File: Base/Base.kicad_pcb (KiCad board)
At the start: 2 copper layers, 0 parts

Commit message: add components
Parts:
- added C1: 22u, Capacitor_THT:CP_Radial_D5.0mm_P2.50mm, F.Cu at (103.0, 97.0)
- added D1: LED, LED_THT:LED_D5.0mm_Clear, F.Cu at (135.0, 102.5)
- added D2: LED, LED_THT:LED_D5.0mm_Clear, F.Cu at (125.0, 102.5)
- added J1: USB_C_Receptacle_PowerOnly_6P, Connector_USB:USB_C_Receptacle_GCT_USB4135-GF-A_6P_TopMnt_Horizontal, F.Cu at (83.5, 78.0)
- added J2: Conn_01x04_Socket, Connector_PinSocket_2.54mm:PinSocket_1x04_P2.54mm_Vertical, F.Cu at (97.0, 89.4)
- added R1: 5k1, Resistor_THT:R_Axial_DIN0207_L6.3mm_D2.5mm_P10.16mm_Horizontal, F.Cu at (89.3, 80.0)
- added R2: 5k1, Resistor_THT:R_Axial_DIN0207_L6.3mm_D2.5mm_P10.16mm_Horizontal, F.Cu at (89.4, 76.0)
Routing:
- net (no net): vias 10 -> 14
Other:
- board outline added: 100 x 40 mm

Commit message: update pcb
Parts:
- added G***: LOGO, LOGO, F.Cu at (176.0, 90.0)

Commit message: RC1
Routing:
- net Net-(D1-K): track 0.00 -> 98.6 mm
- net Net-(D1-A): track 0.00 -> 42.4 mm
- net Net-(J2-Pin_4): track 0.00 -> 32.8 mm
- net Net-(D2-A): track 0.00 -> 31.3 mm
- net Net-(J1-CC1): track 0.00 -> 3.51 mm
- net Net-(J1-CC2): track 0.00 -> 3.43 mm
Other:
- board text added: "JLCJLCJLCJLC"

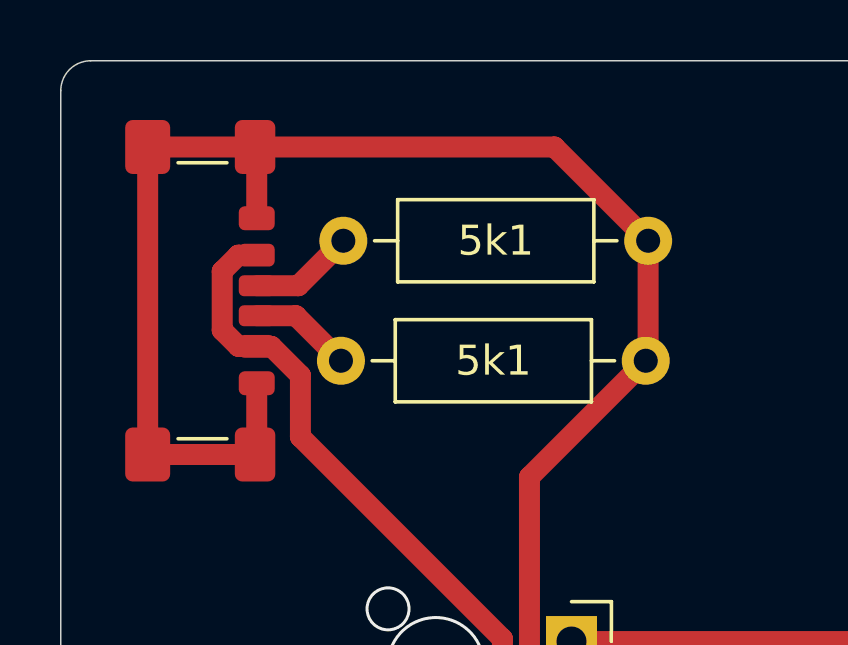
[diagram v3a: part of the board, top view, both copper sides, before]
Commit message: RC2, un-ground shield
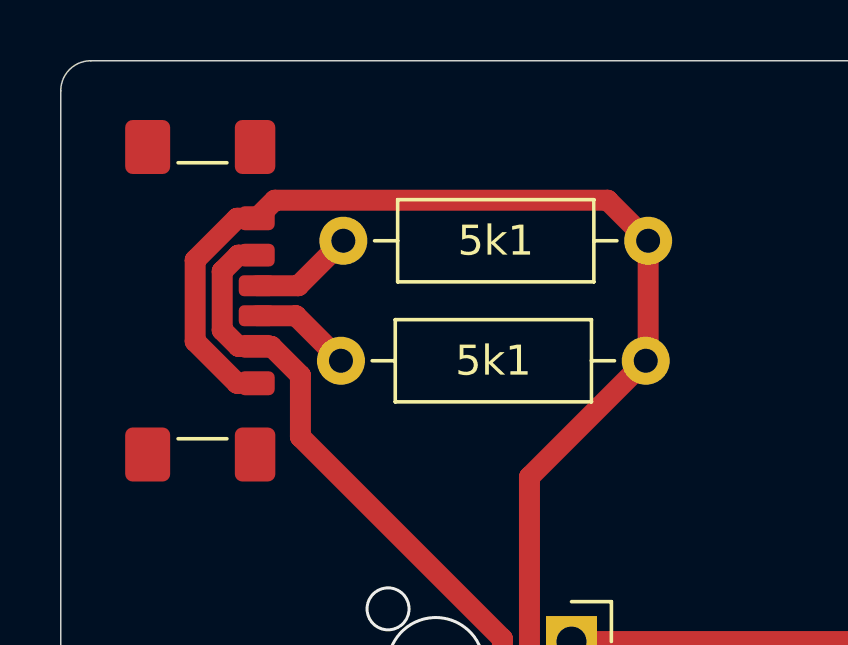
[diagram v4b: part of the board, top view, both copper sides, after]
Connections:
- J1 pad S1: Net-(D1-K) -> unconnected-(J1-SHIELD-PadS1)_3
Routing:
- net Net-(D1-K): track 98.6 -> 83.8 mm
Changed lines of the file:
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@@
 	(net 5 "Net-(J1-CC1)")
 	(net 6 "Net-(J1-CC2)")
+	(net 7 "unconnected-(J1-SHIELD-PadS1)")
+	(net 8 "unconnected-(J1-SHIELD-PadS1)_1")
+	(net 9 "unconnected-(J1-SHIELD-PadS1)_2")
+	(net 10 "unconnected-(J1-SHIELD-PadS1)_3")
 	(footprint "Capacitor_THT:CP_Radial_D5.0mm_P2.50mm"
 		(layer "F.Cu")
@@
 			(layers "F.Cu" "F.Mask" "F.Paste")
 			(roundrect_rratio 0.1851851852)
-			(net 2 "Net-(D1-K)")
+			(net 7 "unconnected-(J1-SHIELD-PadS1)")
 			(pinfunction "SHIELD")
-			(pintype "passive")
+			(pintype "passive+no_connect")
 		)
 		(pad "S1" smd roundrect
@@
 			(layers "F.Cu" "F.Mask" "F.Paste")
 			(roundrect_rratio 0.1666666667)
-			(net 2 "Net-(D1-K)")
+			(net 9 "unconnected-(J1-SHIELD-PadS1)_2")
 			(pinfunction "SHIELD")
-			(pintype "passive")
+			(pintype "passive+no_connect")
 		)
 		(pad "S1" smd roundrect
@@
 			(layers "F.Cu" "F.Mask" "F.Paste")
 			(roundrect_rratio 0.1851851852)
-			(net 2 "Net-(D1-K)")
+			(net 8 "unconnected-(J1-SHIELD-PadS1)_1")
 			(pinfunction "SHIELD")
-			(pintype "passive")
+			(pintype "passive+no_connect")
 		)
 		(pad "S1" smd roundrect
@@
 			(layers "F.Cu" "F.Mask" "F.Paste")
 			(roundrect_rratio 0.1666666667)
-			(net 2 "Net-(D1-K)")
+			(net 10 "unconnected-(J1-SHIELD-PadS1)_3")
 			(pinfunction "SHIELD")
-			(pintype "passive")
+			(pintype "passive+no_connect")
 		)
 		(embedded_fonts no)
@@
 	)
 	(segment
+		(start 86.5325 80.75)
+		(end 85.876726 80.75)
+		(width 0.7)
+		(layer "F.Cu")
+		(net 2)
+	)
+	(segment
 		(start 135 102.54)
 		(end 125 102.54)
@@
 	)
 	(segment
+		(start 84.4805 79.353774)
+		(end 84.480501 76.646225)
+		(width 0.7)
+		(layer "F.Cu")
+		(net 2)
+	)
+	(segment
 		(start 116.7 94.5)
 		(end 103 94.5)
@@
 	)
 	(segment
-		(start 96.455 72.875)
-		(end 86.4775 72.875)
+		(start 84.480501 76.646225)
+		(end 85.876726 75.25)
 		(width 0.7)
 		(layer "F.Cu")
@@
 	)
 	(segment
-		(start 82.8975 83.125)
-		(end 86.4775 83.125)
-		(width 0.7)
-		(layer "F.Cu")
-		(net 2)
-	)
-	(segment
-		(start 86.5325 83.07)
-		(end 86.4775 83.125)
-		(width 0.7)
-		(layer "F.Cu")
-		(net 2)
-	)
-	(segment
-		(start 82.8975 72.875)
-		(end 86.4775 72.875)
+		(start 85.876726 80.75)
+		(end 84.4805 79.353774)
 		(width 0.7)
 		(layer "F.Cu")
@@
 	)
 	(segment
-		(start 86.5325 75.25)
-		(end 86.5325 72.93)
+		(start 87.1335 74.649)
+		(end 98.229 74.649)
 		(width 0.7)
 		(layer "F.Cu")
@@
 	)
 	(segment
-		(start 99.58 76)
-		(end 96.455 72.875)
-		(width 0.7)
-		(layer "F.Cu")
-		(net 2)
-	)
-	(segment
-		(start 86.5325 72.93)
-		(end 86.4775 72.875)
-		(width 0.7)
-		(layer "F.Cu")
-		(net 2)
-	)
-	(segment
-		(start 82.8975 72.875)
-		(end 82.8975 83.125)
+		(start 86.5325 75.25)
+		(end 87.1335 74.649)
 		(width 0.7)
 		(layer "F.Cu")
@@
 	)
 	(segment
-		(start 86.5325 80.75)
-		(end 86.5325 83.07)
+		(start 125 102.54)
+		(end 124.74 102.54)
 		(width 0.7)
 		(layer "F.Cu")
@@
 	)
 	(segment
-		(start 125 102.54)
-		(end 124.74 102.54)
+		(start 85.876726 75.25)
+		(end 86.5325 75.25)
+		(width 0.7)
+		(layer "F.Cu")
+		(net 2)
+	)
+	(segment
+		(start 98.229 74.649)
+		(end 99.58 76)
 		(width 0.7)
 		(layer "F.Cu")
@@
 		(net 6)
 	)
+	(segment
+		(start 86.5325 72.93)
+		(end 86.4775 72.875)
+		(width 0.7)
+		(layer "F.Cu")
+		(net 7)
+	)
+	(segment
+		(start 86.5325 83.07)
+		(end 86.4775 83.125)
+		(width 0.7)
+		(layer "F.Cu")
+		(net 8)
+	)
 	(embedded_fonts no)
